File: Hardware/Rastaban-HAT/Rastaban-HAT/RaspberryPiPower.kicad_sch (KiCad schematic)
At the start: 12 parts, among them IC2 BCM53DS, Q3 DMG2305UX-7

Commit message: started on V0.2 schematic fixes
-fixed vcc on drv8838
-added bypass to backpower protection circuit rpi
-removed unnecessary capacitors
-removed esd ic's
-added esd tvs diodes
-made schematic more readable
-fixed u7 in pcb new(see point 1)
-changed enable focus to hierarchal flag
-stepper motors are 12V only now (removed jumper)
-removed testpoints
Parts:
- added JP?: Jumper_2_Open, symbol Jumper:Jumper_2_Open
- C13: value 100nF 50V -> 100nF 25V
- C7: renamed from C?; value 220u -> 22uF 25V
- gave numbers to parts that had none: 5
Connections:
- net 5VRPI: now also JP?.2 (B)
- net at C13.2, C7.1, IC2.6 (E1)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: now also JP?.1 (A)
- net 12VIN renamed 12V+
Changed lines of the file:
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@@
     (title "Rastaban-HAT")
     (date "2022-11-21")
-    (rev "1.3")
+    (rev "1.4")
     (company "HAN")
     (comment 1 "Casper R. Tak")
@@
   (junction (at 109.22 75.565) (diameter 0) (color 0 0 0 0)
   )
+  (junction (at 168.91 58.42) (diameter 0) (color 0 0 0 0)
+  )
   (junction (at 50.165 60.96) (diameter 0) (color 0 0 0 0)
   )
@@
   (junction (at 100.965 58.42) (diameter 0) (color 0 0 0 0)
   )
+  (junction (at 127.635 58.42) (diameter 0) (color 0 0 0 0)
+  )
   (junction (at 100.965 66.675) (diameter 0) (color 0 0 0 0)
   )
@@
     (stroke (width 0) (type default) (color 0 0 0 0))
   )
-  (wire (pts (xy 50.165 57.15) (xy 50.165 60.96))
-    (stroke (width 0) (type default) (color 0 0 0 0))
-  )
   (wire (pts (xy 100.965 75.565) (xy 109.22 75.565))
     (stroke (width 0) (type default) (color 0 0 0 0))
@@
     (stroke (width 0) (type default) (color 0 0 0 0))
   )
+  (wire (pts (xy 144.145 40.64) (xy 127.635 40.64))
+    (stroke (width 0) (type default) (color 0 0 0 0))
+  )
   (wire (pts (xy 151.765 76.2) (xy 161.925 76.2))
     (stroke (width 0) (type default) (color 0 0 0 0))
@@
     (stroke (width 0) (type default) (color 0 0 0 0))
   )
-  (wire (pts (xy 123.19 58.42) (xy 139.065 58.42))
+  (wire (pts (xy 123.19 58.42) (xy 127.635 58.42))
     (stroke (width 0) (type default) (color 0 0 0 0))
   )
@@
     (stroke (width 0) (type default) (color 0 0 0 0))
   )
-  (wire (pts (xy 161.925 58.42) (xy 170.18 58.42))
+  (wire (pts (xy 154.305 40.64) (xy 168.91 40.64))
+    (stroke (width 0) (type default) (color 0 0 0 0))
+  )
+  (wire (pts (xy 161.925 58.42) (xy 168.91 58.42))
     (stroke (width 0) (type default) (color 0 0 0 0))
   )
@@
     (stroke (width 0) (type default) (color 0 0 0 0))
   )
+  (wire (pts (xy 168.91 58.42) (xy 170.18 58.42))
+    (stroke (width 0) (type default) (color 0 0 0 0))
+  )
   (wire (pts (xy 109.22 62.865) (xy 109.22 58.42))
     (stroke (width 0) (type default) (color 0 0 0 0))
@@
     (stroke (width 0) (type default) (color 0 0 0 0))
   )
+  (wire (pts (xy 127.635 40.64) (xy 127.635 58.42))
+    (stroke (width 0) (type default) (color 0 0 0 0))
+  )
   (wire (pts (xy 161.925 76.2) (xy 161.925 78.74))
     (stroke (width 0) (type default) (color 0 0 0 0))
@@
     (stroke (width 0) (type default) (color 0 0 0 0))
   )
+  (wire (pts (xy 127.635 58.42) (xy 139.065 58.42))
+    (stroke (width 0) (type default) (color 0 0 0 0))
+  )
   (wire (pts (xy 161.925 72.39) (xy 161.925 76.2))
     (stroke (width 0) (type default) (color 0 0 0 0))
@@
   )
   (wire (pts (xy 109.22 58.42) (xy 123.19 58.42))
+    (stroke (width 0) (type default) (color 0 0 0 0))
+  )
+  (wire (pts (xy 168.91 40.64) (xy 168.91 58.42))
     (stroke (width 0) (type default) (color 0 0 0 0))
   )
@@
     (effects (font (size 1.27 1.27)) (justify left bottom))
   )
-  (global_label "12VIN" (shape input) (at 45.72 60.96 180) (fields_autoplaced)
-    (effects (font (size 1.27 1.27)) (justify right))
-    (property "Intersheet References" "${INTERSHEET_REFS}" (id 0) (at 37.864 60.8806 0)
-      (effects (font (size 1.27 1.27)) (justify right) hide)
-    )
-  )
   (hierarchical_label "5VRPI" (shape output) (at 170.18 58.42 0)
     (effects (font (size 1.27 1.27)) (justify left))
   )
-  (hierarchical_label "12V+" (shape input) (at 50.165 57.15 180)
+  (hierarchical_label "12V+" (shape input) (at 45.72 60.96 180)
     (effects (font (size 1.27 1.27)) (justify right))
   )
@@
   )
   (symbol (lib_id "Device:C_Polarized") (at 109.22 66.675 0) (unit 1)
-    (in_bom yes) (on_board yes) (fields_autoplaced)
-    (property "Reference" "C?" (id 0) (at 112.141 64.9513 0)
-      (effects (font (size 1.27 1.27)) (justify left))
-    )
-    (property "Value" "220u" (id 1) (at 112.141 67.4882 0)
+    (in_bom yes) (on_board yes)
+    (property "Reference" "C7" (id 0) (at 109.855 64.135 0)
+      (effects (font (size 1.27 1.27)) (justify left))
+    )
+    (property "Value" "22uF 25V" (id 1) (at 109.855 69.215 0)
       (effects (font (size 1.27 1.27)) (justify left))
     )
@@
   (symbol (lib_id "power:GND") (at 83.185 73.66 0) (unit 1)
     (in_bom yes) (on_board yes) (fields_autoplaced)
-    (property "Reference" "#PWR?" (id 0) (at 83.185 80.01 0)
+    (property "Reference" "#PWR0105" (id 0) (at 83.185 80.01 0)
       (effects (font (size 1.27 1.27)) hide)
     )
@@
   (symbol (lib_id "power:GND") (at 100.965 77.47 0) (unit 1)
     (in_bom yes) (on_board yes) (fields_autoplaced)
-    (property "Reference" "#PWR?" (id 0) (at 100.965 83.82 0)
+    (property "Reference" "#PWR0103" (id 0) (at 100.965 83.82 0)
       (effects (font (size 1.27 1.27)) hide)
     )
@@
     (pin "2")
   )
+  (symbol (lib_id "Jumper:Jumper_2_Open") (at 149.225 40.64 0) (unit 1)
+    (in_bom yes) (on_board yes) (fields_autoplaced)
+    (property "Reference" "JP?" (id 0) (at 149.225 34.29 0))
+    (property "Value" "Jumper_2_Open" (id 1) (at 149.225 36.83 0))
+    (property "Footprint" "" (id 2) (at 149.225 40.64 0)
+      (effects (font (size 1.27 1.27)) hide)
+    )
+    (property "Datasheet" "~" (id 3) (at 149.225 40.64 0)
+      (effects (font (size 1.27 1.27)) hide)
+    )
+    (pin "1")
+    (pin "2")
+  )
   (symbol (lib_id "Device:C") (at 50.165 64.77 0) (unit 1)
     (in_bom yes) (on_board yes)
@@
   (symbol (lib_id "Device:C") (at 123.19 66.04 180) (unit 1)
     (in_bom yes) (on_board yes)
-    (property "Reference" "C13" (id 0) (at 118.745 64.135 0)
+    (property "Reference" "C13" (id 0) (at 123.825 64.135 0)
       (effects (font (size 1.27 1.27)) (justify right))
     )
-    (property "Value" "100nF 50V" (id 1) (at 120.65 69.215 0)
+    (property "Value" "100nF 25V" (id 1) (at 120.65 69.215 0)
       (effects (font (size 1.27 1.27)) (justify right))
     )
@@
   (symbol (lib_id "power:GND") (at 57.15 71.12 0) (mirror y) (unit 1)
     (in_bom yes) (on_board yes) (fields_autoplaced)
-    (property "Reference" "#PWR?" (id 0) (at 57.15 77.47 0)
+    (property "Reference" "#PWR0104" (id 0) (at 57.15 77.47 0)
       (effects (font (size 1.27 1.27)) hide)
     )
@@
   (symbol (lib_id "Device:D_Schottky") (at 83.185 69.85 270) (unit 1)
     (in_bom yes) (on_board yes) (fields_autoplaced)
-    (property "Reference" "D?" (id 0) (at 85.217 68.6978 90)
+    (property "Reference" "D7" (id 0) (at 85.217 68.6978 90)
       (effects (font (size 1.27 1.27)) (justify left))
     )
@@
   (symbol (lib_id "Regulator_Switching:LM2596S-ADJ") (at 69.85 63.5 0) (unit 1)
     (in_bom yes) (on_board yes)
-    (property "Reference" "U?" (id 0) (at 69.977 54.8472 0))
+    (property "Reference" "U5" (id 0) (at 69.977 54.8472 0))
     (property "Value" "LM2596S-ADJ" (id 1) (at 69.977 57.3841 0))
     (property "Footprint" "Package_TO_SOT_SMD:TO-263-5_TabPin3" (id 2) (at 71.12 69.85 0)
@@
   (symbol (lib_id "Device:L") (at 93.98 58.42 90) (unit 1)
     (in_bom yes) (on_board yes) (fields_autoplaced)
-    (property "Reference" "L?" (id 0) (at 93.98 54.2122 90))
+    (property "Reference" "L1" (id 0) (at 93.98 54.2122 90))
     (property "Value" "68uH" (id 1) (at 93.98 56.7491 90))
     (property "Footprint" "Inductor_SMD:L_Bourns-SRU8028_8.0x8.0mm" (id 2) (at 93.98 58.42 0)
@@
   (symbol (lib_id "Device:R") (at 100.965 71.755 0) (unit 1)
     (in_bom yes) (on_board yes) (fields_autoplaced)
-    (property "Reference" "R?" (id 0) (at 102.743 70.9203 0)
+    (property "Reference" "R6" (id 0) (at 102.743 70.9203 0)
       (effects (font (size 1.27 1.27)) (justify left))
     )
@@
   (symbol (lib_id "Device:R") (at 100.965 62.23 0) (unit 1)
     (in_bom yes) (on_board yes) (fields_autoplaced)
-    (property "Reference" "R?" (id 0) (at 102.743 61.3953 0)
-      (effects (font (size 1.27 1.27)) (justify left))
-    )
+    (property "Reference" "R2" (id 0) (at 102.743 61.3953 0)
+      (effects (font (size 1.27 1.27)) (justify left))
+    )

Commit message: removed protection diodes on PGPIO
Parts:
- gave numbers to parts that had none: 1
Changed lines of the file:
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@@
   (symbol (lib_id "Jumper:Jumper_2_Open") (at 149.225 40.64 0) (unit 1)
     (in_bom yes) (on_board yes) (fields_autoplaced)
-    (property "Reference" "JP?" (id 0) (at 149.225 34.29 0))
+    (property "Reference" "JP2" (id 0) (at 149.225 34.29 0))
     (property "Value" "Jumper_2_Open" (id 1) (at 149.225 36.83 0))
     (property "Footprint" "" (id 2) (at 149.225 40.64 0)

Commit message: removed all wiring
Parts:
- D7: footprint (none) -> SamacSys_Parts:SOD2512X110N
- JP2: footprint (none) -> Jumper:SolderJumper-2_P1.3mm_Open_RoundedPad1.0x1.5mm
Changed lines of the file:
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@@
     (property "Reference" "JP2" (id 0) (at 149.225 34.29 0))
     (property "Value" "Jumper_2_Open" (id 1) (at 149.225 36.83 0))
-    (property "Footprint" "" (id 2) (at 149.225 40.64 0)
+    (property "Footprint" "Jumper:SolderJumper-2_P1.3mm_Open_RoundedPad1.0x1.5mm" (id 2) (at 149.225 40.64 0)
       (effects (font (size 1.27 1.27)) hide)
     )
@@
       (effects (font (size 1.27 1.27)) (justify left))
     )
-    (property "Footprint" "" (id 2) (at 83.185 69.85 0)
+    (property "Footprint" "SamacSys_Parts:SOD2512X110N" (id 2) (at 83.185 69.85 0)
       (effects (font (size 1.27 1.27)) hide)
     )

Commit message: finished component placement
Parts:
- C7: footprint Capacitor_SMD:C_0603_1608Metric_Pad1.08x0.95mm_HandSolder -> Capacitor_SMD:C_0805_2012Metric_Pad1.18x1.45mm_HandSolder
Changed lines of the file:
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@@
       (effects (font (size 1.27 1.27)) (justify left))
     )
-    (property "Footprint" "Capacitor_SMD:C_0603_1608Metric_Pad1.08x0.95mm_HandSolder" (id 2) (at 110.1852 70.485 0)
+    (property "Footprint" "Capacitor_SMD:C_0805_2012Metric_Pad1.18x1.45mm_HandSolder" (id 2) (at 110.1852 70.485 0)
       (effects (font (size 1.27 1.27)) hide)
     )

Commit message: started working on V1.4
-changed some footprints
-added/changed some LCSC values to/for components
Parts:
- C13: value 100nF 25V -> 100nF 50V; LCSC C531179 -> C476766
- C7: LCSC (none) -> C5155340
- L1: LCSC (none) -> C82571
- R2, R6: footprint Resistor_SMD:R_0603_1608Metric_Pad0.98x0.95mm_HandSolder -> Resistor_SMD:R_0805_2012Metric_Pad1.20x1.40mm_HandSolder
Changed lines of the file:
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@@
+      (effects (font (size 1.27 1.27)) hide)
+    )
+    (property "LCSC" "C5155340" (id 5) (at 109.22 66.675 0)
       (effects (font (size 1.27 1.27)) hide)
     )
@@
       (effects (font (size 1.27 1.27)) (justify right))
     )
-    (property "Value" "100nF 25V" (id 1) (at 120.65 69.215 0)
+    (property "Value" "100nF 50V" (id 1) (at 120.65 69.215 0)
       (effects (font (size 1.27 1.27)) (justify right))
     )
@@
       (effects (font (size 1.27 1.27)) hide)
     )
-    (property "LCSC" "C531179" (id 4) (at 123.19 66.04 0)
+    (property "LCSC" "C476766" (id 4) (at 123.19 66.04 0)
       (effects (font (size 1.27 1.27)) hide)
     )
@@
       (effects (font (size 1.27 1.27)) hide)
     )
+    (property "LCSC" "C82571" (id 5) (at 93.98 58.42 90)
+      (effects (font (size 1.27 1.27)) hide)
+    )
     (pin "1")
     (pin "2")
@@
       (effects (font (size 1.27 1.27)) (justify left))
     )
-    (property "Footprint" "Resistor_SMD:R_0603_1608Metric_Pad0.98x0.95mm_HandSolder" (id 2) (at 99.187 71.755 90)
+    (property "Footprint" "Resistor_SMD:R_0805_2012Metric_Pad1.20x1.40mm_HandSolder" (id 2) (at 99.187 71.755 90)
       (effects (font (size 1.27 1.27)) hide)
     )
@@
       (effects (font (size 1.27 1.27)) (justify left))
     )
-    (property "Footprint" "Resistor_SMD:R_0603_1608Metric_Pad0.98x0.95mm_HandSolder" (id 2) (at 99.187 62.23 90)
-      (effects (font (size 1.27 1.27)) hide)
-    )
+    (property "Footprint" "Resistor_SMD:R_0805_2012Metric_Pad1.20x1.40mm_HandSolder" (id 2) (at 99.187 62.23 90)
+      (effects (font (size 1.27 1.27)) hide)
+    )

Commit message: improved 4th order list
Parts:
- R2: LCSC (none) -> C17798
- R6: LCSC (none) -> C17557
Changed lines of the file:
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@@
+      (effects (font (size 1.27 1.27)) hide)
+    )
+    (property "LCSC" "C17557" (id 5) (at 100.965 71.755 0)
       (effects (font (size 1.27 1.27)) hide)
     )
@@
       (effects (font (size 1.27 1.27)) hide)
     )
+    (property "LCSC" "C17798" (id 5) (at 100.965 62.23 0)
+      (effects (font (size 1.27 1.27)) hide)
+    )

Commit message: added component on lcsc list
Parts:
- U5: LCSC (none) -> C347423
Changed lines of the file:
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@@
+      (effects (font (size 1.27 1.27)) hide)
+    )
+    (property "LCSC" "C347423" (id 5) (at 69.85 63.5 0)
       (effects (font (size 1.27 1.27)) hide)
     )

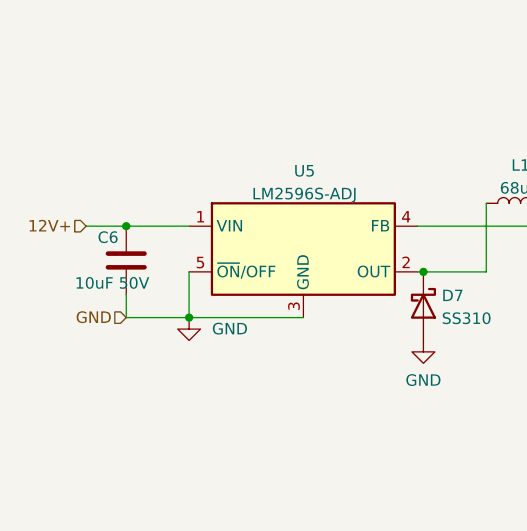
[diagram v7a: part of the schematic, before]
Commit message: improved LCSC + schematic values and order lists
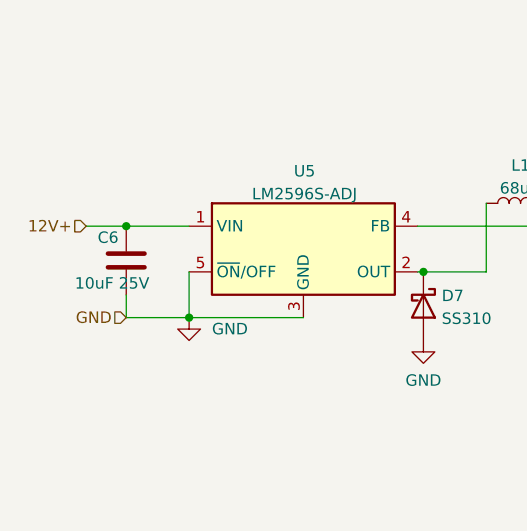
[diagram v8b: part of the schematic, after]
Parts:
- C6: value 10uF 50V -> 10uF 25V; LCSC C17024 -> C15850
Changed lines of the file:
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@@
       (effects (font (size 1.27 1.27)) (justify left))
     )
-    (property "Value" "10uF 50V" (id 1) (at 44.45 67.31 0)
+    (property "Value" "10uF 25V" (id 1) (at 44.45 67.31 0)
       (effects (font (size 1.27 1.27)) (justify left))
     )
@@
       (effects (font (size 1.27 1.27)) hide)
     )
-    (property "LCSC" "C17024" (id 4) (at 50.165 64.77 0)
+    (property "LCSC" "C15850" (id 4) (at 50.165 64.77 0)
       (effects (font (size 1.27 1.27)) hide)
     )
